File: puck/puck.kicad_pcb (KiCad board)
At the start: 2 copper layers, 34 x 34 mm, 12 parts

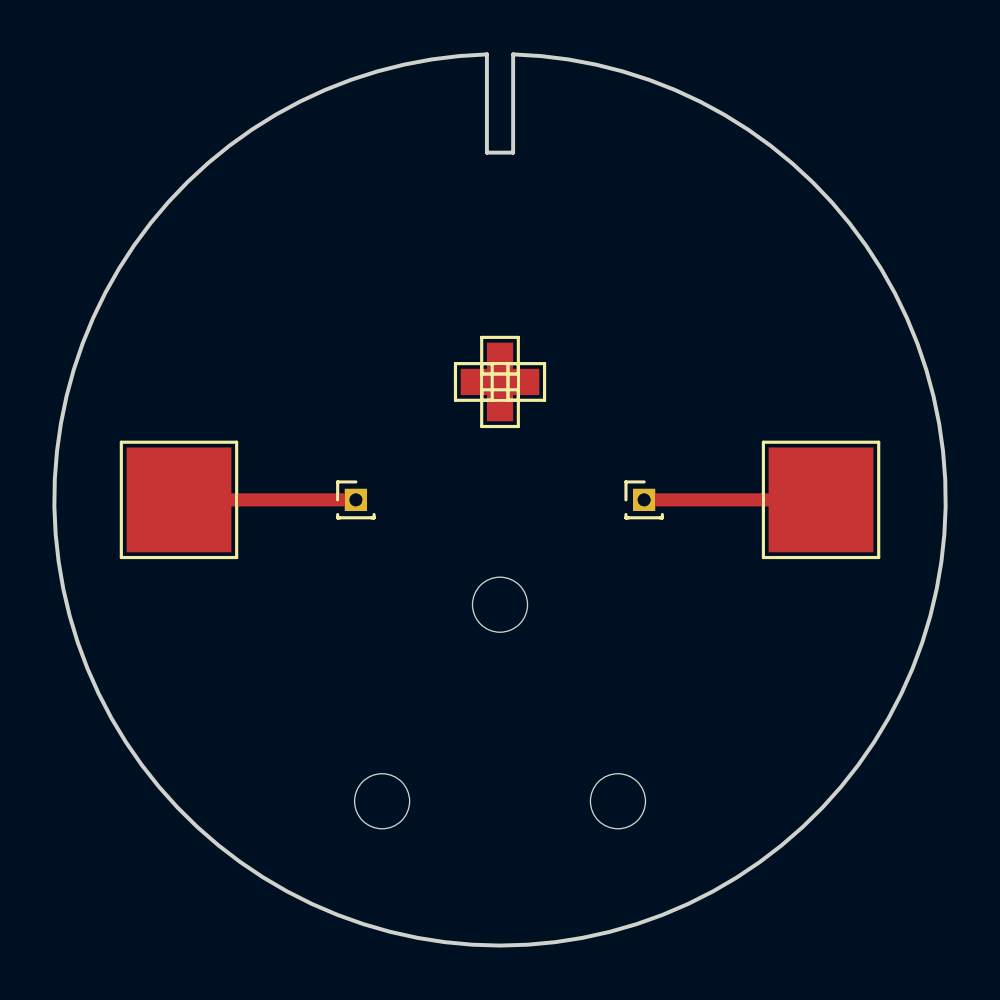
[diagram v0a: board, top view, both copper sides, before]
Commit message: Sized holes, moved lines, set +v indicator
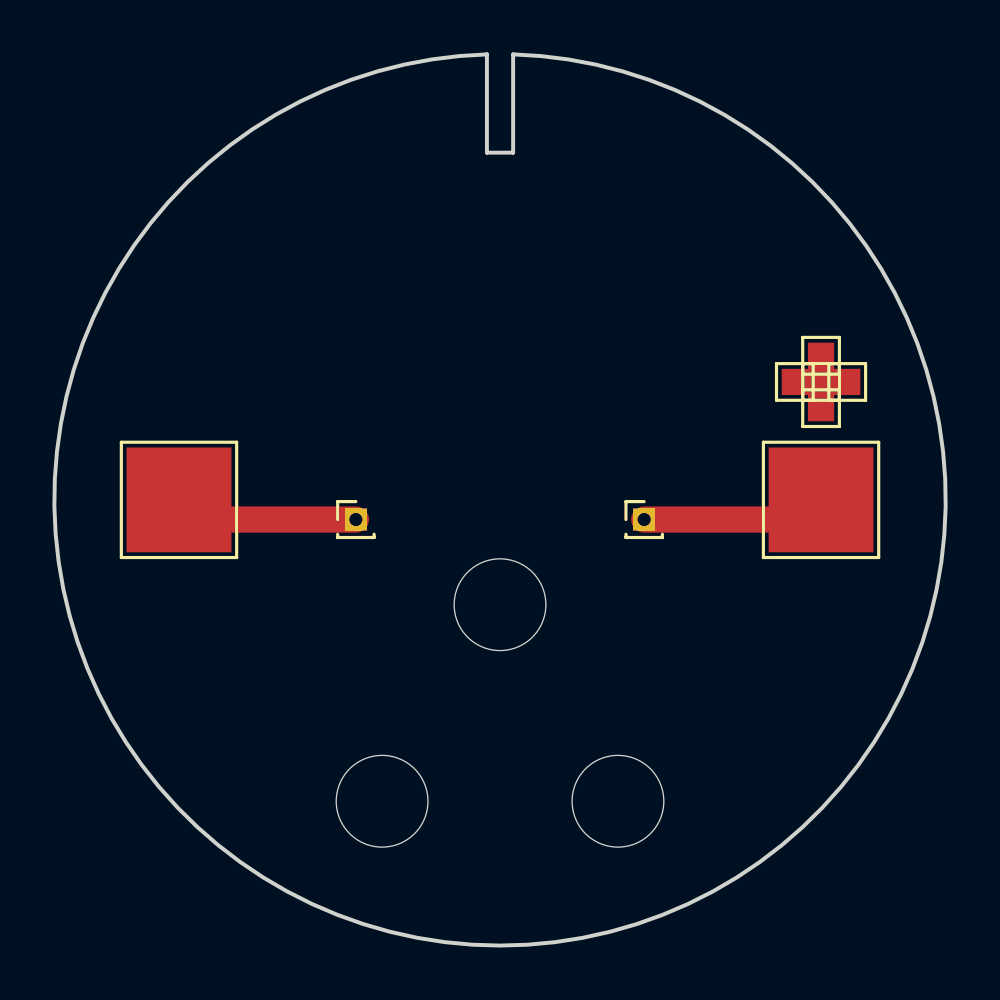
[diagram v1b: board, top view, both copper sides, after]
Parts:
- removed the REF** at (49.0, 45.5)
- removed the REF** at (50.0, 46.5)
- removed the REF** at (51.0, 45.5)
- removed the REF** at (50.0, 44.5)
- removed the REF** at (50.0, 45.5)
- added REF**: TestPoint_Pad_1.0x1.0mm, TestPoint:TestPoint_Pad_1.0x1.0mm, F.Cu at (61.2, 45.5)
- added REF**: TestPoint_Pad_1.0x1.0mm, TestPoint:TestPoint_Pad_1.0x1.0mm, F.Cu at (62.2, 46.5)
- added REF**: TestPoint_Pad_1.0x1.0mm, TestPoint:TestPoint_Pad_1.0x1.0mm, F.Cu at (63.2, 45.5)
- added REF**: TestPoint_Pad_1.0x1.0mm, TestPoint:TestPoint_Pad_1.0x1.0mm, F.Cu at (62.2, 44.5)
- added REF**: TestPoint_Pad_1.0x1.0mm, TestPoint:TestPoint_Pad_1.0x1.0mm, F.Cu at (62.2, 45.5)
- moved REF** 0.75 mm to (44.5, 50.8)
- moved REF** 0.75 mm to (55.5, 50.8)
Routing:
- net (no net): track 13.5 -> 14.1 mm
